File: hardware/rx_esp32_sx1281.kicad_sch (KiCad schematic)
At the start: 25 parts, among them SW1 SKUBAAE010, U16 ESP32-PICO-V3, U18 SX1281, X3 52MHz TCXO

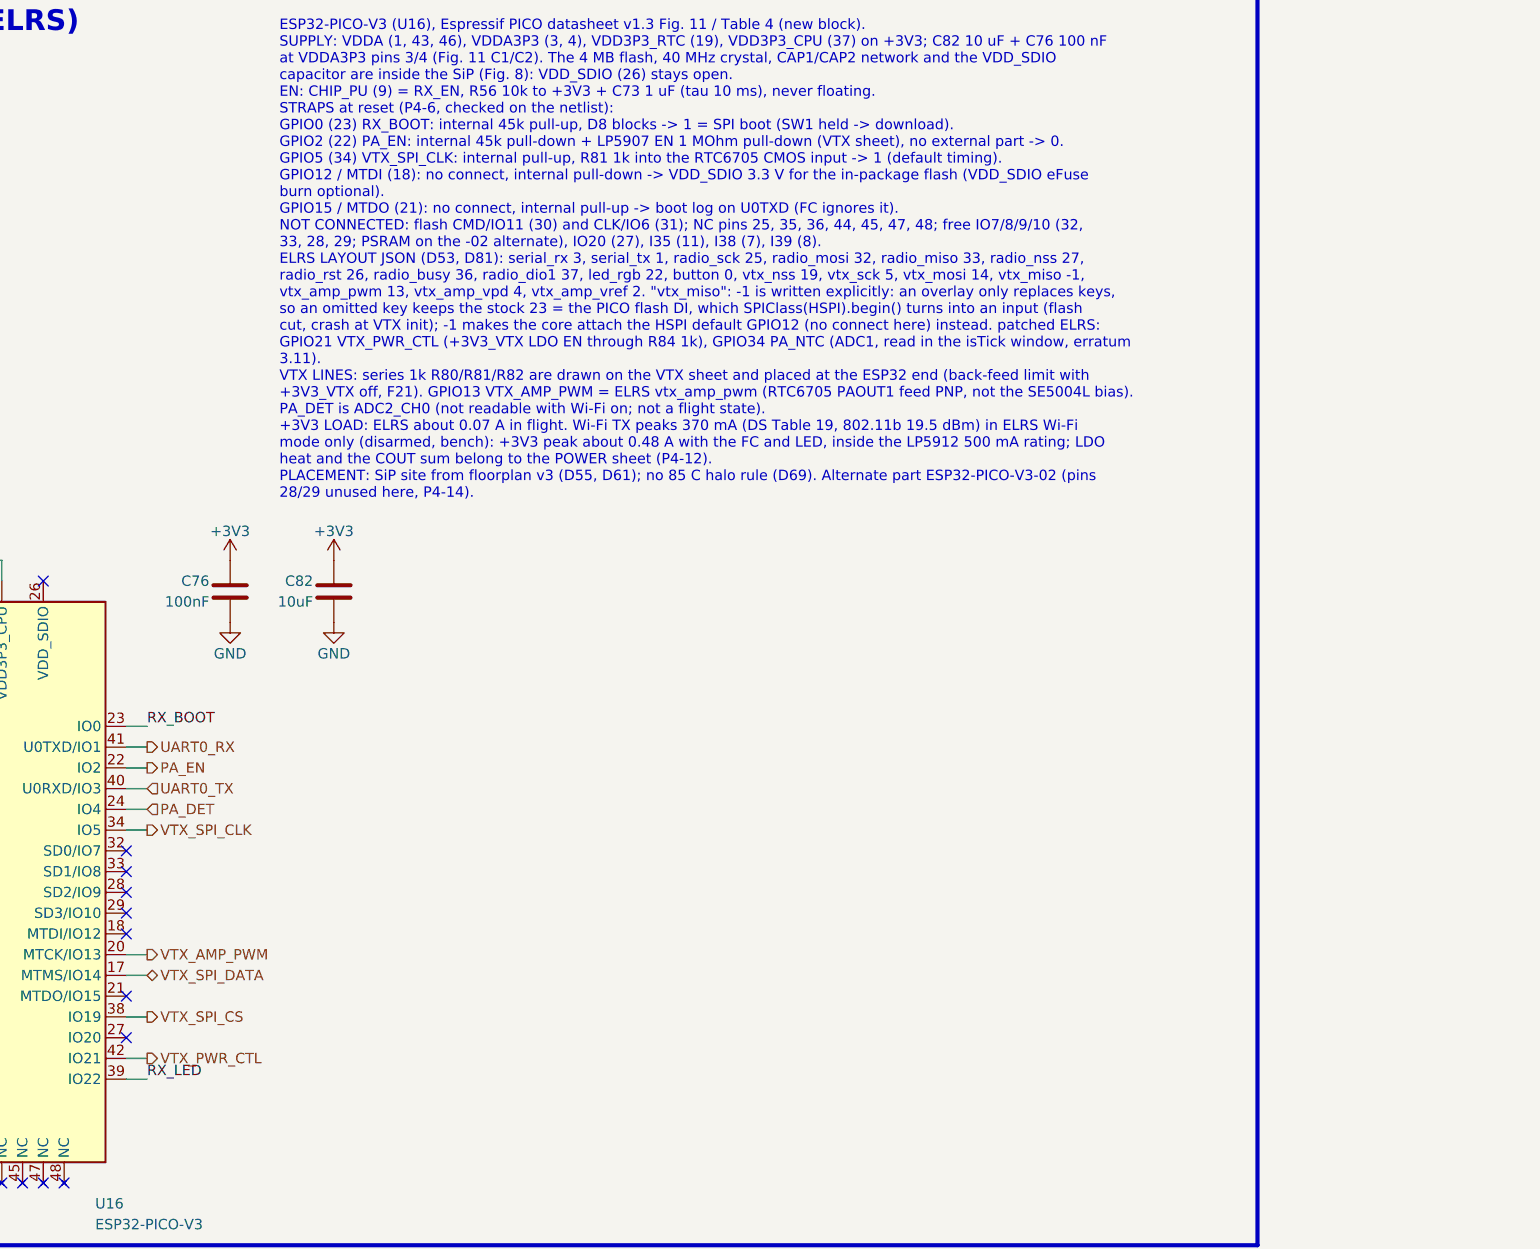
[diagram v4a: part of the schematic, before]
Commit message: wip: routing prep (zones and via fields) and schematic review round 4
Co-Authored-By: Claude Opus 5.5 <noreply@anthropic.com>
Claude-Session: https://claude.ai/code/session_01RFaS5jnC9tnPam9GBgmGnG
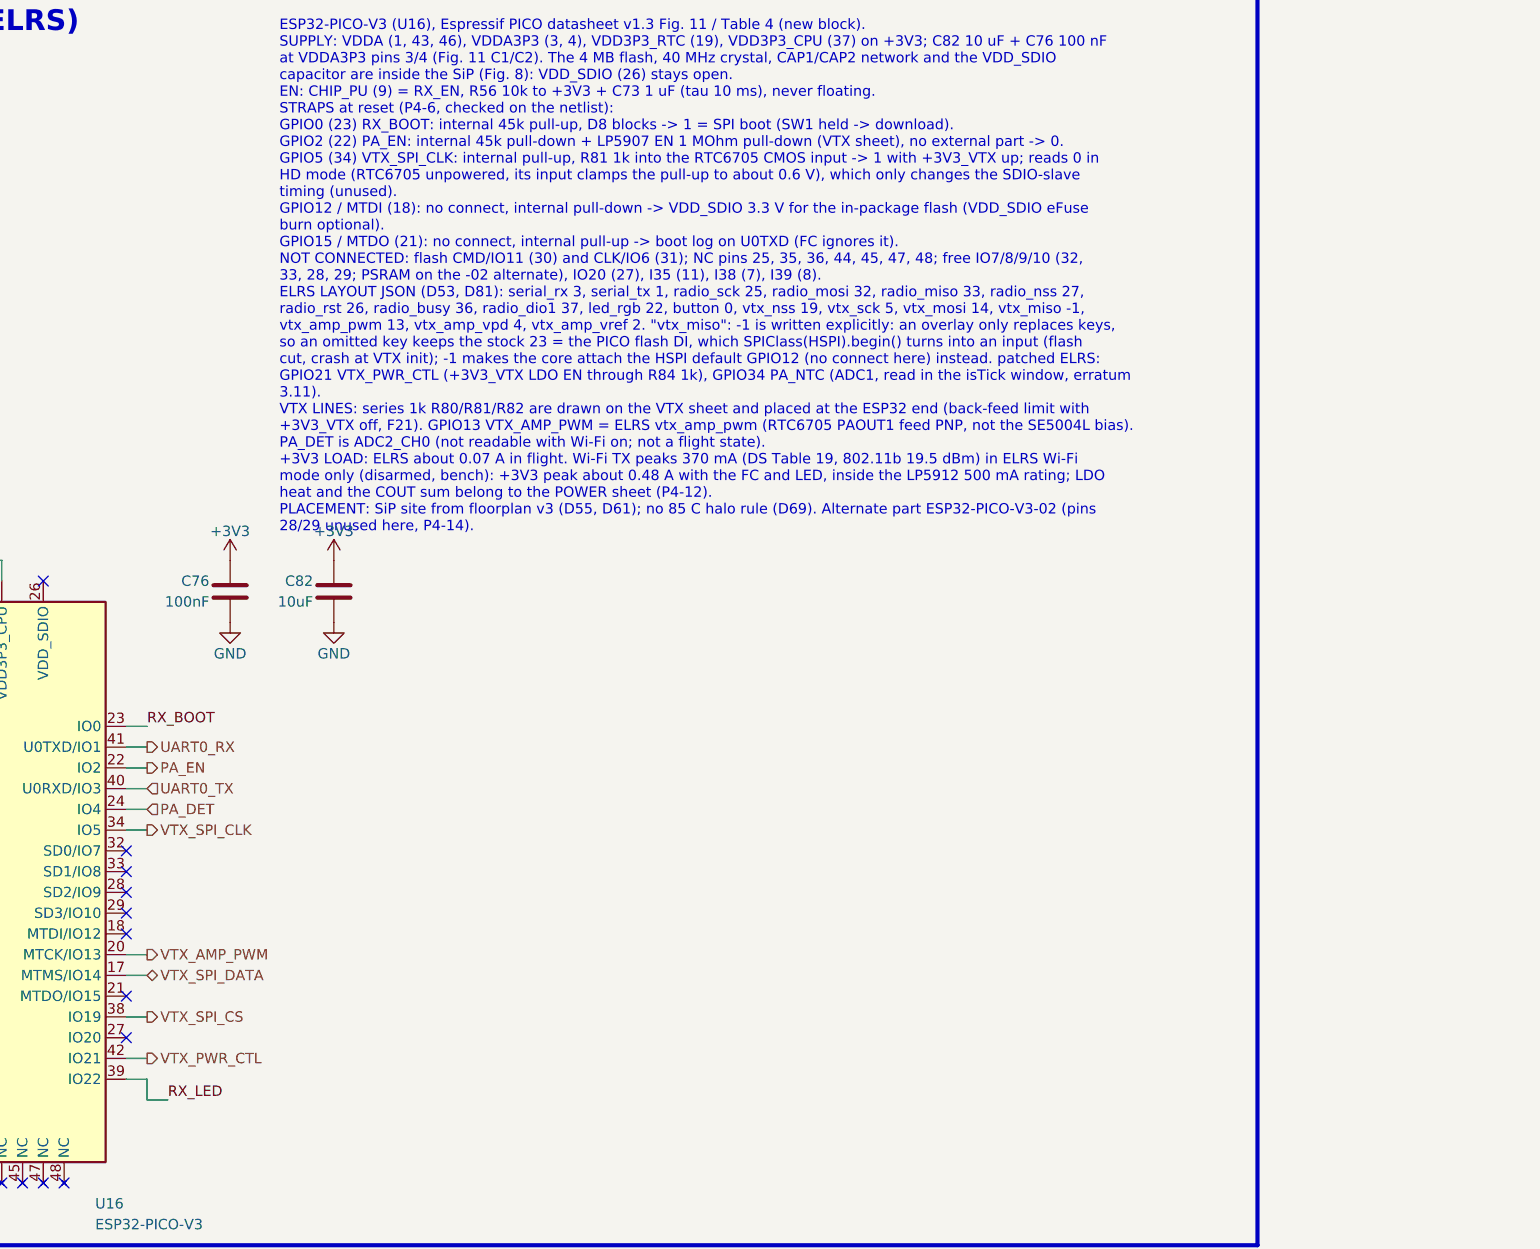
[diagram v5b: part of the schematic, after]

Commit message: schematic: review complete (4 rounds; U20 pin 1 to GND, footprint filters fixed, TPS22810DRVR, R54 270R); ERC 0 errors, check_netlist 7/7; D85-D87
Co-Authored-By: Claude Opus 5.5 <noreply@anthropic.com>
Claude-Session: https://claude.ai/code/session_01RFaS5jnC9tnPam9GBgmGnG
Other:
- moved on the sheet: C76, C82
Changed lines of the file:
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@@
 		)
 	)
-	(text_box "Wi-Fi (D58): LNA_IN (2) -> RF_WIFI 50 Ohm CPW <= 8 mm -> C133 shunt (DNP) / R88 0R series (fitted) / C132 shunt (DNP) -> AE2 Johanson 2450AT07A0100001T (FEED 1/4, GND 2/3). Same pi as Espressif Fig. 11 (C4/L1/C3) and OpenRX-Lite-UFL (C22/L2/C21). The PICO matches LNA_IN to 50 Ohm inside, so the network only tunes the antenna: values from V7 tuning (VNA at the feed or Johanson's service); R88 may become a Murata LQP03TN 0201 inductor. The AE2 footprint carries the 5.0 x 3.2 mm keep-out (DRU 'D21 wifi_antenna_edge_strip')."
+	(text_box "Wi-Fi (D58): LNA_IN (2) -> RF_WIFI 50 Ohm line (<= 8 mm preferred, D69; FLOORPLAN open item 10) -> C133 shunt (DNP) / R88 0R series (fitted) / C132 shunt (DNP) -> AE2 Johanson 2450AT07A0100001T (FEED 1/4, GND 2/3). Same pi as Espressif Fig. 11 (C4/L1/C3) and OpenRX-Lite-UFL (C22/L2/C21). The PICO matches LNA_IN to 50 Ohm inside, so the network only tunes the antenna: values from V7 tuning (VNA at the feed or Johanson's service); R88 may become a Murata LQP03TN 0201 inductor. The AE2 footprint carries the 5.0 x 3.2 mm keep-out (DRU 'D21 wifi_antenna_edge_strip')."
 		(exclude_from_sim no)
 		(at 152.4 208.28 0)
@@
 	(symbol
 		(lib_id "Device:C")
-		(at 279.4 171.45 0)
+		(at 292.1 186.69 0)
 		(unit 1)
 		(body_style 1)
@@
 		(dnp no)
 		(property "Reference" "C76"
-			(at 276.86 170.18 0)
+			(at 289.56 185.42 0)
 			(show_name no)
 			(do_not_autoplace no)
@@
 		)
 		(property "Value" "100nF"
-			(at 276.86 172.72 0)
+			(at 289.56 187.96 0)
 			(show_name no)
 			(do_not_autoplace no)
@@
 		)
 		(property "Footprint" "lib:C_0201_0603Metric_W"
-			(at 279.4 171.45 0)
+			(at 292.1 186.69 0)
 			(hide yes)
 			(show_name no)
@@
 		)
 		(property "Datasheet" ""
-			(at 279.4 171.45 0)
+			(at 292.1 186.69 0)
 			(hide yes)
 			(show_name no)
@@
 		)
 		(property "Description" "Unpolarized capacitor"
-			(at 279.4 171.45 0)
+			(at 292.1 186.69 0)
 			(hide yes)
 			(show_name no)
@@
 		)
 		(property "LCSC" "C181047"
-			(at 279.4 171.45 0)
+			(at 292.1 186.69 0)
 			(hide yes)
 			(show_name no)
@@
 		)
 		(property "MPN" "GRM033C81E104KE14D"
-			(at 279.4 171.45 0)
+			(at 292.1 186.69 0)
 			(hide yes)
 			(show_name no)
@@
 		)
 		(property "Manufacturer" "Murata"
-			(at 279.4 171.45 0)
+			(at 292.1 186.69 0)
 			(hide yes)
 			(show_name no)
@@
 	(symbol
 		(lib_id "power:GND")
-		(at 279.4 175.26 0)
+		(at 292.1 190.5 0)
 		(unit 1)
 		(body_style 1)
@@
 		(in_pos_files no)
 		(dnp no)
-		(property "Reference" "#PWR175"
-			(at 279.4 181.61 0)
+		(property "Reference" "#PWR176"
+			(at 292.1 196.85 0)
 			(hide yes)
 			(show_name no)
@@
 		)
 		(property "Value" "GND"
-			(at 279.4 179.07 0)
+			(at 292.1 194.31 0)
 			(show_name no)
 			(do_not_autoplace no)
@@
 		)
 		(property "Footprint" ""
-			(at 279.4 175.26 0)
+			(at 292.1 190.5 0)
 			(hide yes)
 			(show_name no)
@@
 		)
 		(property "Datasheet" ""
-			(at 279.4 175.26 0)
+			(at 292.1 190.5 0)
 			(hide yes)
 			(show_name no)
@@
 		)
 		(property "Description" "Power symbol creates a global label with name \"GND\" , ground"
-			(at 279.4 175.26 0)
+			(at 292.1 190.5 0)
 			(hide yes)
 			(show_name no)
@@
 			(project "OpenAIO-Whoop"
 				(path "/2c3a7206-1e66-4d43-a02f-491225e20dd6/73d8a02c-e770-5e7b-9535-3e34b447ded8"
-					(reference "#PWR175")
+					(reference "#PWR176")
 					(unit 1)
 				)
@@
 	(symbol
 		(lib_id "power:GND")
-		(at 292.1 175.26 0)
+		(at 304.8 190.5 0)
 		(unit 1)
 		(body_style 1)
@@
 		(in_pos_files no)
 		(dnp no)
-		(property "Reference" "#PWR176"
-			(at 292.1 181.61 0)
+		(property "Reference" "#PWR177"
+			(at 304.8 196.85 0)
 			(hide yes)
 			(show_name no)
@@
 		)
 		(property "Value" "GND"
-			(at 292.1 179.07 0)
+			(at 304.8 194.31 0)
 			(show_name no)
 			(do_not_autoplace no)
@@
 		)
 		(property "Footprint" ""
-			(at 292.1 175.26 0)
+			(at 304.8 190.5 0)
 			(hide yes)
 			(show_name no)
@@
 		)
 		(property "Datasheet" ""
-			(at 292.1 175.26 0)
+			(at 304.8 190.5 0)
 			(hide yes)
 			(show_name no)
@@
 		)
 		(property "Description" "Power symbol creates a global label with name \"GND\" , ground"
-			(at 292.1 175.26 0)
+			(at 304.8 190.5 0)
 			(hide yes)
 			(show_name no)
@@
 			(project "OpenAIO-Whoop"
 				(path "/2c3a7206-1e66-4d43-a02f-491225e20dd6/73d8a02c-e770-5e7b-9535-3e34b447ded8"
-					(reference "#PWR176")
+					(reference "#PWR177")
 					(unit 1)
 				)
@@
 	(symbol
 		(lib_id "Device:C")
-		(at 292.1 171.45 0)
+		(at 304.8 186.69 0)
 		(unit 1)
 		(body_style 1)
@@
 		(dnp no)
 		(property "Reference" "C82"
-			(at 289.56 170.18 0)
+			(at 302.26 185.42 0)
 			(show_name no)
 			(do_not_autoplace no)
@@
 		)
 		(property "Value" "10uF"
-			(at 289.56 172.72 0)
+			(at 302.26 187.96 0)
 			(show_name no)
 			(do_not_autoplace no)
@@
 		)
 		(property "Footprint" "lib:C_0402_1005Metric_W"
-			(at 292.1 171.45 0)
+			(at 304.8 186.69 0)
 			(hide yes)
 			(show_name no)
@@
 		)
 		(property "Datasheet" ""
-			(at 292.1 171.45 0)
+			(at 304.8 186.69 0)
 			(hide yes)
 			(show_name no)
@@
 		)
 		(property "Description" "Unpolarized capacitor"
-			(at 292.1 171.45 0)
+			(at 304.8 186.69 0)
 			(hide yes)
 			(show_name no)
@@
 		)
 		(property "LCSC" "C237279"
-			(at 292.1 171.45 0)
+			(at 304.8 186.69 0)
 			(hide yes)
 			(show_name no)
@@
 		)
 		(property "MPN" "GRM155C80J106ME11D"
-			(at 292.1 171.45 0)
+			(at 304.8 186.69 0)
 			(hide yes)
 			(show_name no)
@@
 		)
 		(property "Manufacturer" "Murata"
-			(at 292.1 171.45 0)
+			(at 304.8 186.69 0)
 			(hide yes)
 			(show_name no)
@@
 		(in_pos_files no)
 		(dnp no)
-		(property "Reference" "#PWR177"
+		(property "Reference" "#PWR175"
 			(at 207.01 191.77 0)
 			(hide yes)
@@
 			(project "OpenAIO-Whoop"
 				(path "/2c3a7206-1e66-4d43-a02f-491225e20dd6/73d8a02c-e770-5e7b-9535-3e34b447ded8"
-					(reference "#PWR177")
+					(reference "#PWR175")
 					(unit 1)
 				)
@@
 	(symbol
 		(lib_id "power:+3V3")
-		(at 292.1 167.64 0)
+		(at 304.8 182.88 0)
 		(unit 1)
 		(body_style 1)
@@
 		(in_pos_files no)
 		(dnp no)
-		(property "Reference" "#PWR173"
-			(at 292.1 171.45 0)
+		(property "Reference" "#PWR174"
+			(at 304.8 186.69 0)
 			(hide yes)
 			(show_name no)
@@
 		)
 		(property "Value" "+3V3"
-			(at 292.1 164.084 0)
+			(at 304.8 179.324 0)
 			(show_name no)
 			(do_not_autoplace no)
@@
 		)
 		(property "Footprint" ""
-			(at 292.1 167.64 0)
+			(at 304.8 182.88 0)
 			(hide yes)
 			(show_name no)
@@
 		)
 		(property "Datasheet" ""
-			(at 292.1 167.64 0)
+			(at 304.8 182.88 0)
 			(hide yes)
 			(show_name no)
@@
 		)
 		(property "Description" "Power symbol creates a global label with name \"+3V3\""
-			(at 292.1 167.64 0)
+			(at 304.8 182.88 0)
 			(hide yes)
 			(show_name no)
@@
 			(project "OpenAIO-Whoop"
 				(path "/2c3a7206-1e66-4d43-a02f-491225e20dd6/73d8a02c-e770-5e7b-9535-3e34b447ded8"
-					(reference "#PWR173")
+					(reference "#PWR174")
 					(unit 1)
 				)
@@
 	(symbol
 		(lib_id "power:+3V3")
-		(at 279.4 167.64 0)
+		(at 292.1 182.88 0)
 		(unit 1)
 		(body_style 1)
@@
 		(in_pos_files no)
 		(dnp no)
-		(property "Reference" "#PWR172"
-			(at 279.4 171.45 0)
+		(property "Reference" "#PWR173"
+			(at 292.1 186.69 0)
 			(hide yes)
 			(show_name no)
@@
 		)
 		(property "Value" "+3V3"
-			(at 279.4 164.084 0)
+			(at 292.1 179.324 0)
 			(show_name no)
 			(do_not_autoplace no)
@@
 		)
 		(property "Footprint" ""
-			(at 279.4 167.64 0)
+			(at 292.1 182.88 0)
 			(hide yes)
 			(show_name no)
@@
 		)
 		(property "Datasheet" ""
-			(at 279.4 167.64 0)
+			(at 292.1 182.88 0)
 			(hide yes)
 			(show_name no)
@@
 		)
 		(property "Description" "Power symbol creates a global label with name \"+3V3\""
-			(at 279.4 167.64 0)
+			(at 292.1 182.88 0)
 			(hide yes)
 			(show_name no)
@@
 			(project "OpenAIO-Whoop"
 				(path "/2c3a7206-1e66-4d43-a02f-491225e20dd6/73d8a02c-e770-5e7b-9535-3e34b447ded8"
-					(reference "#PWR172")
+					(reference "#PWR173")
 					(unit 1)
 				)
@@
 		(in_pos_files no)
 		(dnp no)
-		(property "Reference" "#PWR174"
+		(property "Reference" "#PWR172"
 			(at 213.36 173.99 0)
 			(hide yes)
@@
 			(project "OpenAIO-Whoop"
 				(path "/2c3a7206-1e66-4d43-a02f-491225e20dd6/73d8a02c-e770-5e7b-9535-3e34b447ded8"
-					(reference "#PWR174")
+					(reference "#PWR172")
 					(unit 1)
 				)

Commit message: WIP final schematic (D111/D113): GPIO map, D100 oscillator, final footprints, lineup power-net names; mid-run snapshot, not yet verified (ERC/netlist/DRU regen pending)
Co-Authored-By: Claude Opus 5.5 <noreply@anthropic.com>
Claude-Session: https://claude.ai/code/session_01RFaS5jnC9tnPam9GBgmGnG
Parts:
- AE2: footprint lib:ANT-SMD_4P-L1.0-W0.5_Johanson_2450AT07A0100_Edge5.0x3.2 -> lib:ANT-SMD_4P-L1.0-W0.5_Johanson_2450AT07A0100
- C132, C133, C73, C76, C83, C84, C85, C86, C87, C88, C89, C91, C92: footprint lib:C_0201_0603Metric_W -> lib:C_0201_0603Metric_L
- C82: footprint lib:C_0402_1005Metric_W -> lib:C_0402_1005Metric_L
- R56, R88: footprint lib:R_0201_0603Metric_W -> lib:R_0201_0603Metric_L
- U16: footprint lib:LGA-48_7x7mm_P0.5mm_EP_ESP32-PICO -> lib:LGA-48_7x7mm_P0.5mm_EP_ESP32-PICO_L
- U18: footprint lib:QFN-24_L4.0-W4.0-P0.50-TL-EP2.6_Dense -> lib:QFN-24_L4.0-W4.0-P0.50-TL-EP2.6_L
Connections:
- net PA_DET: now also U16.5 (SENSOR_VP/I36); no longer U16.24 (IO4)
- net PA_EN: now also U16.42 (IO21); no longer U16.22 (IO2)
- net PA_NTC: now also U16.6 (SENSOR_CAPP/I37); no longer U16.10 (VDET_1/I34)
- net RADIO_BUSY: now also U16.8 (SENSOR_VN/I39); no longer U16.5 (SENSOR_VP/I36)
- net RADIO_DIO1: now also U16.10 (VDET_1/I34); no longer U16.6 (SENSOR_CAPP/I37)
- net RADIO_MISO: now also U16.20 (MTCK/IO13); no longer U16.13 (32K_XN/IO33)
- net RADIO_MOSI: now also U16.17 (MTMS/IO14); no longer U16.12 (32K_XP/IO32)
- net RADIO_NSS: now also U16.15 (IO26); no longer U16.16 (IO27)
- net RADIO_RST: now also U16.14 (IO25); no longer U16.15 (IO26)
- net RADIO_SCK: now also U16.16 (IO27); no longer U16.14 (IO25)
- net RX_LED: now also U16.12 (32K_XP/IO32); no longer U16.39 (IO22)
- net VTX_AMP_PWM: now also U16.13 (32K_XN/IO33); no longer U16.20 (MTCK/IO13)
- net VTX_PWR_CTL: now also U16.24 (IO4); no longer U16.42 (IO21)
- net VTX_SPI_CLK: now also U16.27 (IO20); no longer U16.34 (IO5)
- net VTX_SPI_CS: now also U16.39 (IO22); no longer U16.38 (IO19)
- net VTX_SPI_DATA: now also U16.38 (IO19); no longer U16.17 (MTMS/IO14)
- net +3V3 renamed +3.3V
